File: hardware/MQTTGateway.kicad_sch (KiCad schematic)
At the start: 0 parts

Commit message: Add ethernet, WIFI, LEDs, CAN, RS485, RS232 etc.
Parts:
- added FID? (x4): Fiducial, symbol Mechanical:Fiducial
- added H? (x4): MountingHole_Pad, MountingHole:MountingHole_3.2mm_M3_DIN965_Pad, symbol Mechanical:MountingHole_Pad
- added U1: W25Q128JVS, Package_SO:SOIC-8_5.3x5.3mm_P1.27mm, symbol Memory_Flash:W25Q128JVS
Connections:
- new net GND: H?.1, H?.1, H?.1, H?.1
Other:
- added sheet Ethernet (Ethernet.kicad_sch)
- added sheet Inputs (Inputs.kicad_sch)
- added sheet MCU (Microcontroller_Unit.kicad_sch)
- added sheet Outputs (Outputs.kicad_sch)
- added sheet PSU (Power_Supply_Unit.kicad_sch)
- added sheet Peripherals (Peripherals.kicad_sch)
- added sheet WIFI (WIFI.kicad_sch)
- company: (none) -> FEYTECH PTY LTD
- title: (none) -> MQTT Gateway

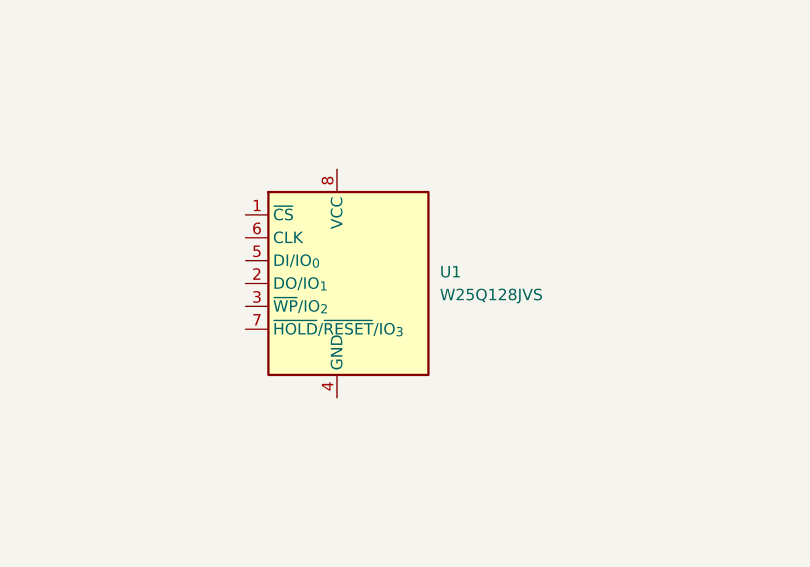
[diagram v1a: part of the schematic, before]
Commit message: Change ESP32 module to stand-alone, change regulator for wide input range, modify location of certain things on MCU_Unit.
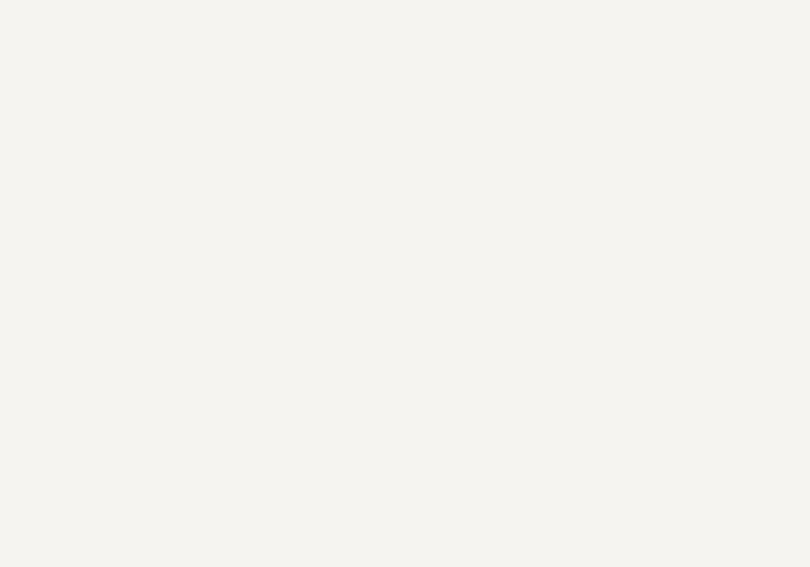
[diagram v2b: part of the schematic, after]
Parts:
- removed U1: W25Q128JVS, Package_SO:SOIC-8_5.3x5.3mm_P1.27mm, symbol Memory_Flash:W25Q128JVS
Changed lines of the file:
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@@
-	)
-	(symbol
-		(lib_id "Memory_Flash:W25Q128JVS")
-		(at 200.66 78.74 0)
-		(unit 1)
-		(exclude_from_sim no)
-		(in_bom yes)
-		(on_board yes)
-		(dnp no)
-		(fields_autoplaced yes)
-		(property "Reference" "U1"
-			(at 212.09 77.4699 0)
-			(effects
-				(font
-					(size 1.27 1.27)
-				)
-				(justify left)
-			)
-		)
-		(property "Value" "W25Q128JVS"
-			(at 212.09 80.0099 0)
-			(effects
-				(font
-					(size 1.27 1.27)
-				)
-				(justify left)
-			)
-		)
-		(property "Footprint" "Package_SO:SOIC-8_5.3x5.3mm_P1.27mm"
-			(at 200.66 55.88 0)
-			(effects
-				(font
-					(size 1.27 1.27)
-				)
-				(hide yes)
-			)
-		)
-		(property "Datasheet" "https://www.winbond.com/resource-files/w25q128jv_dtr%20revc%2003272018%20plus.pdf"
-			(at 200.66 53.34 0)
-			(effects
-				(font
-					(size 1.27 1.27)
-				)
-				(hide yes)
-			)
-		)
-		(property "Description" "128Mbit / 16MiB Serial Flash Memory, Standard/Dual/Quad SPI, 2.7-3.6V, SOIC-8"
-			(at 200.66 50.8 0)
-			(effects
-				(font
-					(size 1.27 1.27)
-				)
-				(hide yes)
-			)
-		)
-		(pin "6"
-		)
-		(pin "3"
-		)
-		(pin "5"
-		)
-		(pin "2"
-		)
-		(pin "1"
-		)
-		(pin "4"
-		)
-		(pin "8"
-		)
-		(pin "7"
-		)
-		(instances
-			(project "MQTTGateway"
-				(path "/05707d4e-3d4a-41f6-9822-862f6f3b507e"
-					(reference "U1")
-					(unit 1)
-				)
-			)
-		)
 	)
 	(symbol

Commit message: Improvements to schematic.
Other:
- added sheet Inputs_Iso (Inputs_Iso.kicad_sch)
- added sheet Outputs_ISOL (Outputs_ISOL.kicad_sch)
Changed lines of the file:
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@@
+	)
+	(sheet
+		(at 167.64 43.18)
+		(size 22.86 33.02)
+		(exclude_from_sim no)
+		(in_bom yes)
+		(on_board yes)
+		(dnp no)
+		(fields_autoplaced yes)
+		(stroke
+			(width 0.1524)
+			(type solid)
+		)
+		(fill
+			(color 0 0 0 0.0000)
+		)
+		(property "Sheetname" "Inputs_Iso"
+			(at 167.64 42.4684 0)
+			(effects
+				(font
+					(size 1.27 1.27)
+				)
+				(justify left bottom)
+			)
+		)
+		(property "Sheetfile" "Inputs_Iso.kicad_sch"
+			(at 167.64 76.7846 0)
+			(effects
+				(font
+					(size 1.27 1.27)
+				)
+				(justify left top)
+			)
+		)
+		(instances
+			(project "MQTTGateway"
+				(path "/05707d4e-3d4a-41f6-9822-862f6f3b507e"
+					(page "9")
+				)
+			)
+		)
+	)
+	(sheet
+		(at 167.64 82.55)
+		(size 22.86 22.86)
+		(exclude_from_sim no)
+		(in_bom yes)
+		(on_board yes)
+		(dnp no)
+		(fields_autoplaced yes)
+		(stroke
+			(width 0.1524)
+			(type solid)
+		)
+		(fill
+			(color 0 0 0 0.0000)
+		)
+		(property "Sheetname" "Outputs_ISOL"
+			(at 167.64 81.8384 0)
+			(effects
+				(font
+					(size 1.27 1.27)
+				)
+				(justify left bottom)
+			)
+		)
+		(property "Sheetfile" "Outputs_ISOL.kicad_sch"
+			(at 167.64 105.9946 0)
+			(effects
+				(font
+					(size 1.27 1.27)
+				)
+				(justify left top)
+			)
+		)
+		(instances
+			(project "MQTTGateway"
+				(path "/05707d4e-3d4a-41f6-9822-862f6f3b507e"
+					(page "10")
+				)
+			)
+		)
 	)
 	(sheet

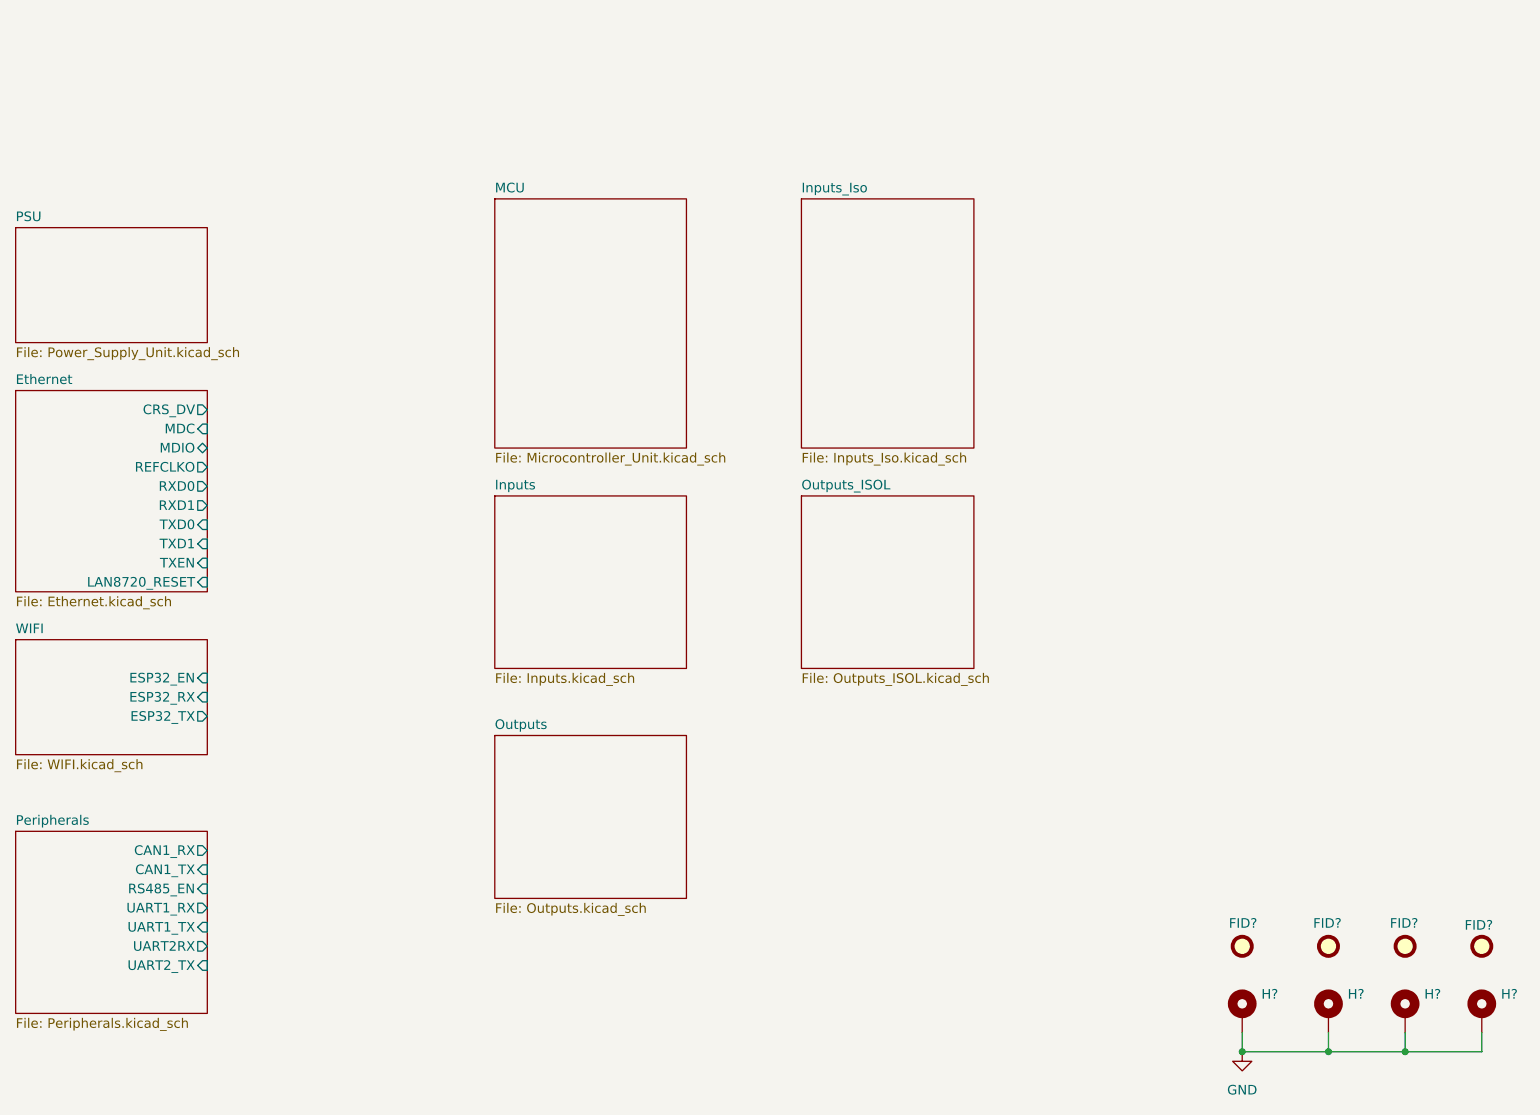
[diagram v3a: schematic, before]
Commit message: Add footprint to components
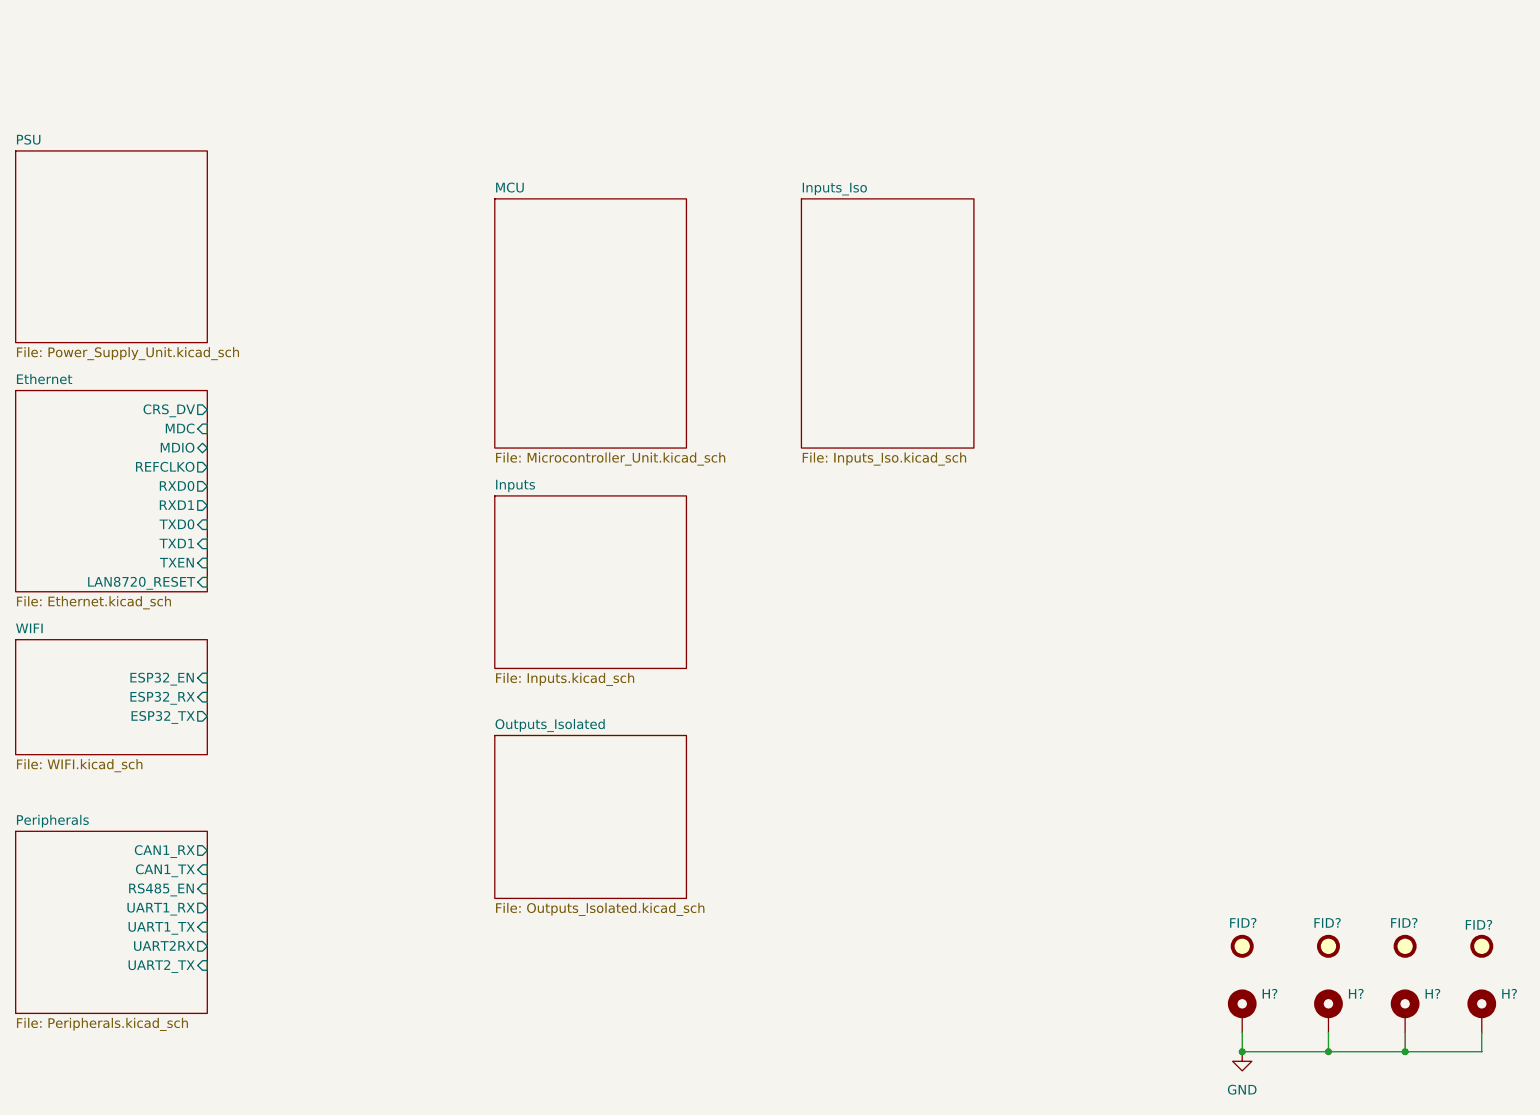
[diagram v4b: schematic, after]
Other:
- sheet Outputs renamed Outputs_Isolated
- removed sheet Outputs_ISOL
- sheet Outputs_Isolated: file Outputs.kicad_sch -> Outputs_Isolated.kicad_sch
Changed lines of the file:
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@@
-	)
-	(sheet
-		(at 167.64 82.55)
-		(size 22.86 22.86)
-		(exclude_from_sim no)
-		(in_bom yes)
-		(on_board yes)
-		(dnp no)
-		(fields_autoplaced yes)
-		(stroke
-			(width 0.1524)
-			(type solid)
-		)
-		(fill
-			(color 0 0 0 0.0000)
-		)
-		(property "Sheetname" "Outputs_ISOL"
-			(at 167.64 81.8384 0)
-			(effects
-				(font
-					(size 1.27 1.27)
-				)
-				(justify left bottom)
-			)
-		)
-		(property "Sheetfile" "Outputs_ISOL.kicad_sch"
-			(at 167.64 105.9946 0)
-			(effects
-				(font
-					(size 1.27 1.27)
-				)
-				(justify left top)
-			)
-		)
-		(instances
-			(project "MQTTGateway"
-				(path "/05707d4e-3d4a-41f6-9822-862f6f3b507e"
-					(page "10")
-				)
-			)
-		)
 	)
 	(sheet
@@
 			(color 0 0 0 0.0000)
 		)
-		(property "Sheetname" "Outputs"
+		(property "Sheetname" "Outputs_Isolated"
 			(at 127 113.5884 0)
 			(effects
@@
 			)
 		)
-		(property "Sheetfile" "Outputs.kicad_sch"
+		(property "Sheetfile" "Outputs_Isolated.kicad_sch"
 			(at 127 136.4746 0)
 			(effects
@@
 	)
 	(sheet
-		(at 63.5 46.99)
-		(size 25.4 15.24)
+		(at 63.5 36.83)
+		(size 25.4 25.4)
 		(exclude_from_sim no)
 		(in_bom yes)
@@
 		)
 		(property "Sheetname" "PSU"
-			(at 63.5 46.2784 0)
-			(effects
-				(font
+			(at 63.5 36.1184 0)
+			(effects
+				(font

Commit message: Improvements
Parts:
- FID1, FID2, FID3, FID4: renamed from FID?; footprint (none) -> Fiducial:Fiducial_0.5mm_Mask1.5mm
- gave numbers to parts that had none: 4
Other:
- sheet Inputs ports: added ANALOG1, ANALOG2, ANALOG3, ANALOG4, Digital_In_1, Digital_In_2, Digital_In_3, Digital_In_4; removed none
- sheet Inputs_Iso ports: added DIG_IN_ISO_1, DIG_IN_ISO_2, DIG_IN_ISO_3, DIG_IN_ISO_4; removed none
- sheet MCU ports: added ANALOG1, ANALOG2, ANALOG3, ANALOG4, CAN1_RX, CAN1_TX, CRS_DV, DIG_IN_ISO_1, DIG_IN_ISO_2, DIG_IN_ISO_3, DIG_IN_ISO_4, Digital_In_1, Digital_In_2, Digital_In_3, Digital_In_4, ESP32_EN, ESP32_RX, ESP32_TX, LAN8720_RESET, MDC, MDIO, OUTPUT_ISO1, OUTPUT_ISO2, OUTPUT_ISO3, OUTPUT_ISO4, REFCLKO, RS485_EN, RXD0, RXD1, TXD0, TXD1, TXEN, UART1_RX, UART1_TX, UART2_RX, UART2_TX; removed none
- sheet Outputs_Isolated ports: added OUTPUT_ISO1, OUTPUT_ISO2, OUTPUT_ISO3, OUTPUT_ISO4; removed none
- sheet Peripherals ports: added UART2_RX; removed UART2RX
